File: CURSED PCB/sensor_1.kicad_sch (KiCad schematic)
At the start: 18 parts, among them J1 Micro_SD_Card, J3 Conn_01x05_Socket, U5 PIC18F26K22-xSO, U8 MCP2562-H-P, Y1 Crystal

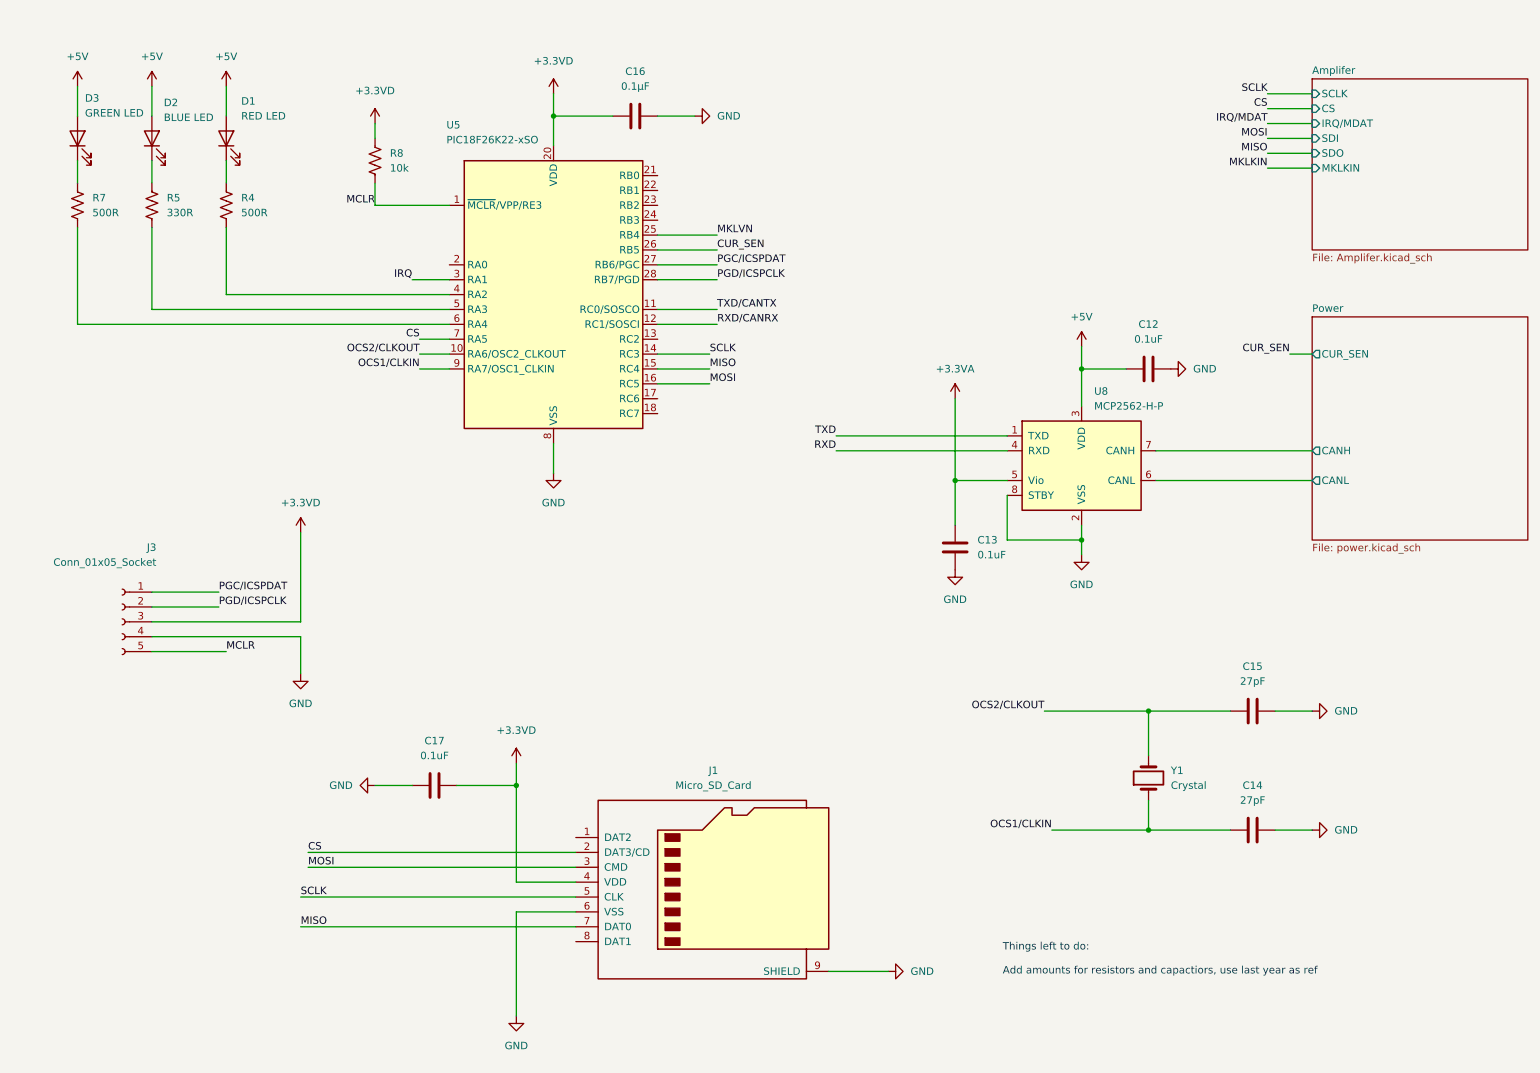
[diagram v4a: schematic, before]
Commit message: Added reference voltage and some other stuff
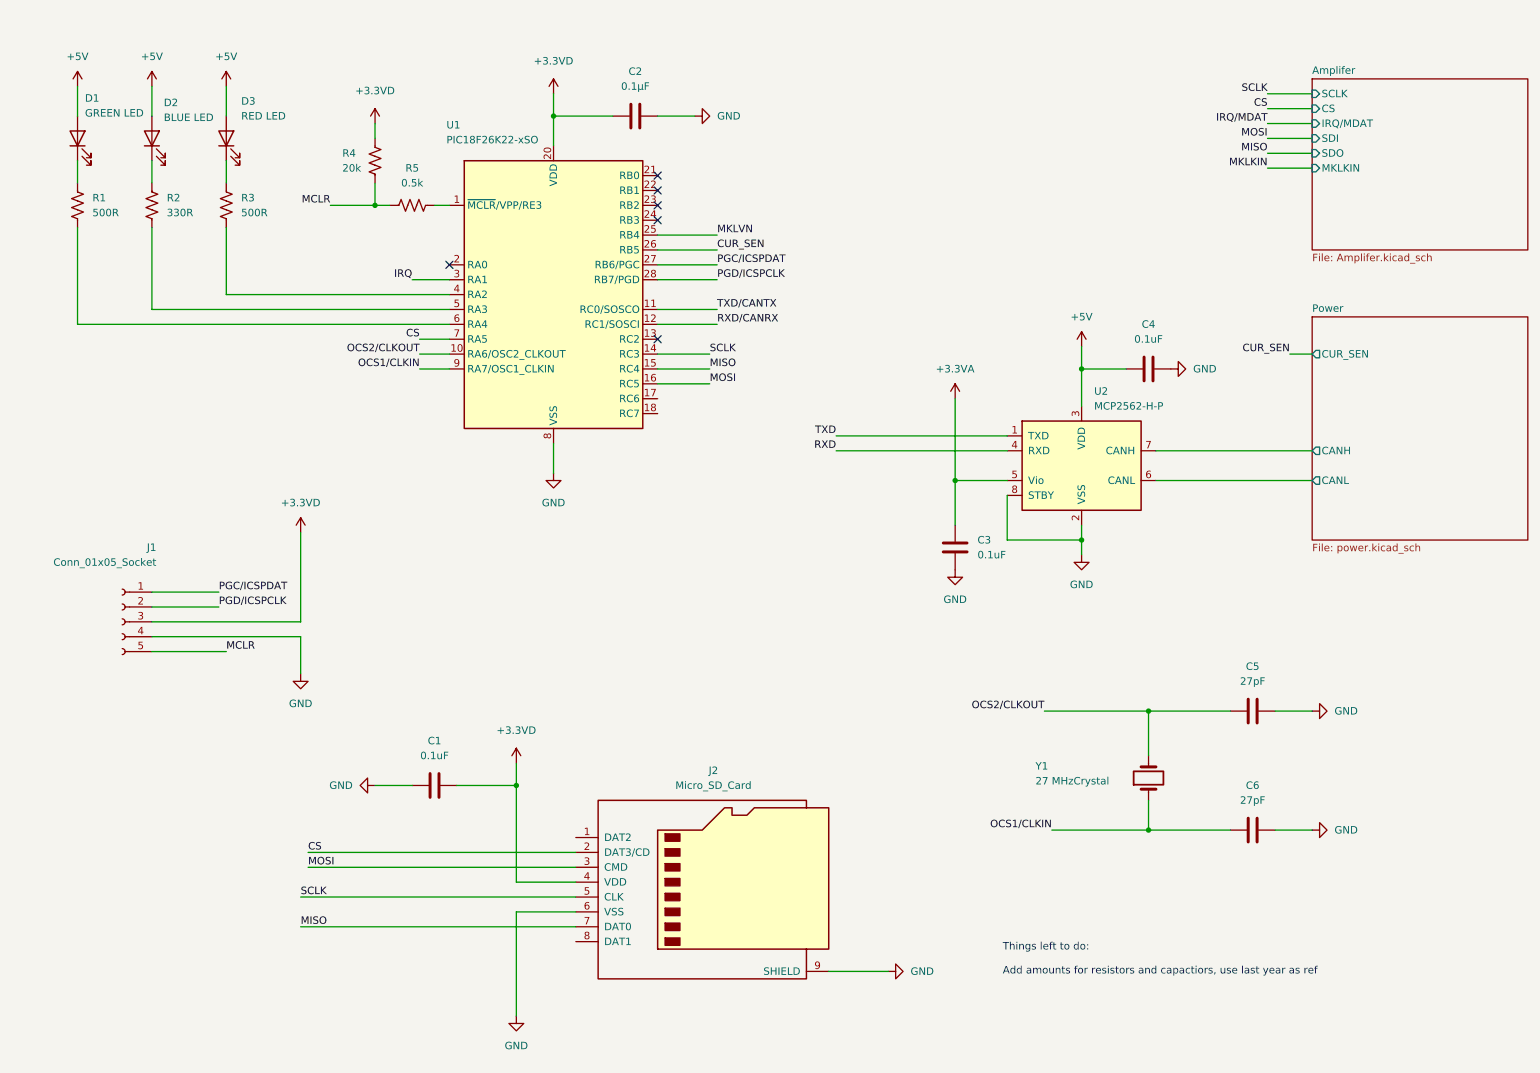
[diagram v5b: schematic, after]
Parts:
- added R5: 0.5k, Resistor_SMD:R_0201_0603Metric, symbol Device:R_US
- C1: renamed from C17; footprint PCM_Capacitor_SMD_AKL:C_0201_0603Metric -> Capacitor_SMD:C_0201_0603Metric_Pad0.64x0.40mm_HandSolder
- C2: renamed from C16; footprint PCM_Capacitor_SMD_AKL:C_0201_0603Metric -> Capacitor_SMD:C_0201_0603Metric_Pad0.64x0.40mm_HandSolder
- C3: renamed from C13; footprint PCM_Capacitor_SMD_AKL:C_0201_0603Metric -> Capacitor_SMD:C_0201_0603Metric_Pad0.64x0.40mm_HandSolder
- C4: renamed from C12; footprint PCM_Capacitor_SMD_AKL:C_0201_0603Metric -> Capacitor_SMD:C_0201_0603Metric_Pad0.64x0.40mm_HandSolder
- C5: renamed from C15; footprint PCM_Capacitor_SMD_AKL:C_0201_0603Metric -> Capacitor_SMD:C_0201_0603Metric_Pad0.64x0.40mm_HandSolder
- C6: renamed from C14; footprint PCM_Capacitor_SMD_AKL:C_0201_0603Metric -> Capacitor_SMD:C_0201_0603Metric_Pad0.64x0.40mm_HandSolder
- D1: renamed from D3; footprint (none) -> LED_SMD:LED_0201_0603Metric
- D2: footprint (none) -> LED_SMD:LED_0201_0603Metric
- D3: renamed from D1; footprint (none) -> LED_SMD:LED_0201_0603Metric
- J1: renamed from J3; footprint (none) -> canhw_footprints:PinSocket_5x2.54_SMD_90deg_952-3198-1-ND
- J2: renamed from J1; footprint (none) -> canhw_footprints:microSD_Molex_WM6698CT-ND
- R1: renamed from R7; footprint (none) -> Resistor_SMD:R_0201_0603Metric
- R2: renamed from R5; footprint (none) -> Resistor_SMD:R_0201_0603Metric
- R3: renamed from R4; footprint (none) -> Resistor_SMD:R_0201_0603Metric
- R4: renamed from R8; value 10k -> 20k; footprint (none) -> Resistor_SMD:R_0201_0603Metric
- Y1: value Crystal -> 27 MHzCrystal; footprint (none) -> Crystal:Crystal_HC49-4H_Vertical
- renumbered U5 to U1, U8 to U2
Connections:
- net MCLR: now also R5.1; no longer U1.1 (~{MCLR}/VPP/RE3)
- new net: R5.2, U1.1 (~{MCLR}/VPP/RE3)
- no-connect marks 0 -> 6

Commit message: Changes to stuff
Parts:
- removed R5: 0.5k, Resistor_SMD:R_0201_0603Metric, symbol Device:R_US
- removed U1: PIC18F26K22-xSO, Package_SO:SOIC-28W_7.5x17.9mm_P1.27mm, symbol MCU_Microchip_PIC18:PIC18F26K22-xSO
- removed U2: MCP2562-H-P, Package_DIP:DIP-8_W7.62mm, symbol Interface_CAN_LIN:MCP2562-H-P
- added JP1, JP2, JP3: Jumper, symbol Jumper:Jumper_2_Small_Bridged
- added Q?: PZTA42, Package_TO_SOT_SMD:SOT-223-3_TabPin2, symbol Transistor_BJT:PZTA42
- added U10: MCP2562, symbol canhw:MCP2562
- added U9: PIC18F26K83, symbol canhw:PIC18F26K83
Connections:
- net +3.3VA: now also U10.5 (VIO)
- net +3.3VD: now also U9.20 (VDD)
- net +5V: now also JP1.2 (B), JP2.2 (B), JP3.2 (B), U10.3 (VDD); no longer D1.2 (A), D2.2 (A), D3.2 (A)
- net CS: now also U9.7 (RA5)
- net CUR_SEN: now also U9.26 (RB5)
- net GND: now also U10.2 (VSS), U10.8 (STBY)
- net IRQ: now also U9.3 (RA1)
- net MCLR: now also U9.1 (~{MCLR})
- net MISO: now also U9.22 (RB1)
- net MKLVN: now also U9.25 (RB4)
- net MOSI: now also U9.23 (RB2)
- net OCS1/CLKIN: now also U9.9 (RA7/OSC1)
- net OCS2/CLKOUT: now also U9.10 (RA6/OSC2)
- net PGC/ICSPDAT: now also U9.28 (RB7/ICSPDAT)
- net PGD/ICSPCLK: now also U9.27 (RB6/ICSPCLK)
- net Power/CANH: now also U10.7 (CANH)
- net Power/CANL: now also U10.6 (CANL)
- net RXD: now also U10.4 (RXD)
- net RXD/CANRX: now also U9.17 (RC6)
- net SCLK: now also U9.8 (VSS)
- net TXD: now also U10.1 (TXD)
- net TXD/CANTX: now also U9.18 (RC7)
- net at R3.2: now also U9.4 (RA2)
- net at R2.2: now also U9.5 (RA3)
- net at R1.2: now also U9.6 (RA4)
- new net: D3.2 (A), JP3.1 (A)
- new net: D1.2 (A), JP1.1 (A)
- new net: D2.2 (A), JP2.1 (A)
- no-connect marks 6 -> 2
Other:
- note added: "page done"
- note removed: "Things left to do: Add amounts for resistors and capactiors, use last year as ref"
- moved on the sheet: C2, R3, R4

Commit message: fixed issue with mcu
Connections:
- net SCLK: now also U9.14 (RC3); no longer U9.8 (VSS)
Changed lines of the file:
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@@
+	(wire
+		(pts
+			(xy 87.63 71.12) (xy 80.01 71.12)
+		)
+		(stroke
+			(width 0)
+			(type default)
+		)
+	)
 	(wire
 		(pts
@@
 		(pts
 			(xy 175.26 86.36) (xy 186.69 86.36)
-		)
-		(stroke
-			(width 0)
-			(type default)
-		)
-	)
-	(wire
-		(pts
-			(xy 124.46 71.12) (xy 133.35 71.12)
 		)
 		(stroke
@@
 	)
 	(label "SCLK"
-		(at 133.35 71.12 0)
-		(effects
-			(font
+		(at 80.01 71.12 0)
+		(effects
+			(font

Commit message: something something fixes to something related
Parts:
- added U12: AD5761BRUZ, AD5761BRUZ:SOP65P640X120-16N, symbol AD5761BRUZ:AD5761BRUZ
- gave numbers to parts that had none: 1
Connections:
- net +3.3VA: now also U12.4 (VREFIN), U12.8 (VDD)
- net +3.3VD: now also U12.15 (DVCC)
- net +5V: now also D1.1 (K), D2.1 (K), D3.1 (K), R1.1, R2.1, R3.1
- net CS: now also U12.13 (~{SYNC})
- net GND: now also U12.16 (DGND), U12.5 (AGND), U12.6 (VSS)
- net MISO: now also U12.10 (SDO)
- net MOSI: now also U12.12 (SDI)
- net SCLK: now also U12.14 (SCLK)
- net at Q1.1 (B): now also U12.7 (VOUT)
- no-connect marks 2 -> 6
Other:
- moved on the sheet: C1, D2, D3, J2, JP1, JP2, JP3, Q1, R1, R2
